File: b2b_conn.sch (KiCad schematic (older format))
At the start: 3 parts

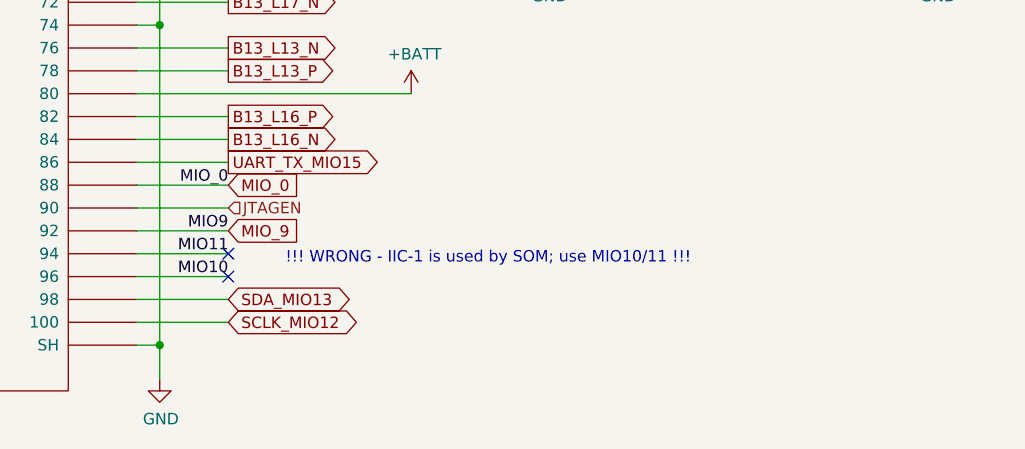
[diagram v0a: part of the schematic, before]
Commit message: re-routed i2c from mio12/13 -> mio10/11
Fixed bug; mio12/13 is used internally on the SOM.
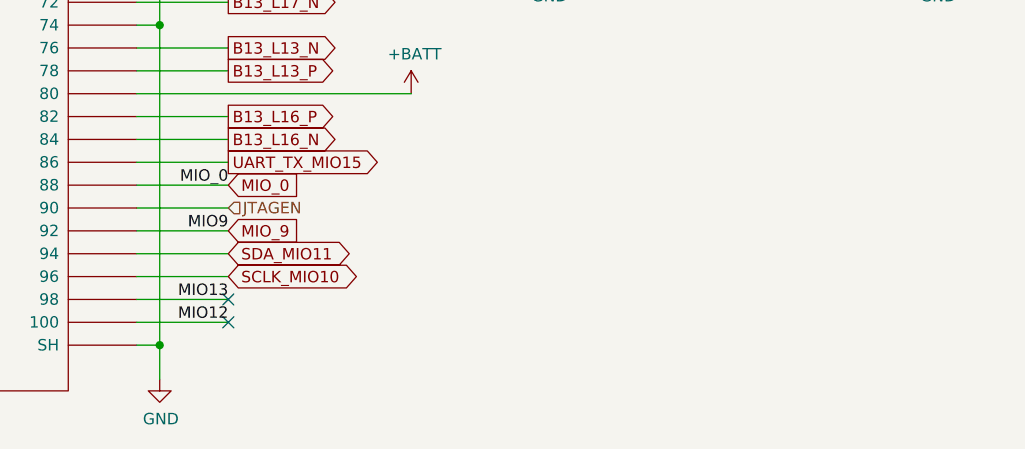
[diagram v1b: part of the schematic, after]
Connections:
- net MIO10 renamed SCLK_MIO10
- net MIO11 renamed SDA_MIO11
- net SCLK_MIO12 renamed MIO12
- net SDA_MIO13 renamed MIO13
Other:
- note removed: "!!! WRONG - IIC-1 is used by SOM; use MIO10/11 !!!"
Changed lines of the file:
@@
 Text GLabel 1300 5700 0    50   Input ~ 0
 UART_RX_MIO14
-Text GLabel 3600 6000 2    50   BiDi ~ 0
-SDA_MIO13
-Text GLabel 3600 6100 2    50   BiDi ~ 0
-SCLK_MIO12
 Text GLabel 6800 1800 2    50   Input ~ 0
 MGT_RX1_N
@@
 Text Label 3600 5700 2    50   ~ 0
 MIO9
-Text Label 3600 5800 2    50   ~ 0
-MIO11
-Text Label 3600 5900 2    50   ~ 0
-MIO10
-NoConn ~ 3600 5800
-NoConn ~ 3600 5900
 NoConn ~ 1300 6000
 NoConn ~ 1300 6100
@@
 Text GLabel 3600 5700 2    50   Input ~ 0
 MIO_9
-Text Notes 3850 5850 0    50   ~ 0
-!!! WRONG - IIC-1 is used by SOM; use MIO10/11 !!!
+Text Label 3600 6000 2    50   ~ 0
+MIO13
+Text Label 3600 6100 2    50   ~ 0
+MIO12
+Text GLabel 3600 5900 2    50   BiDi ~ 0
+SCLK_MIO10
+Text GLabel 3600 5800 2    50   BiDi ~ 0
+SDA_MIO11
+NoConn ~ 3600 6000
+NoConn ~ 3600 6100
 $EndSCHEMATC
